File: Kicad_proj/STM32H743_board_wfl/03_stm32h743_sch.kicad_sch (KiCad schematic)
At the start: 1 part, among them U1 STM32H743VITx

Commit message: v0.3 uzupelniony prebom + placement BMI088 na sch
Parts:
- renumbered U1 to U3
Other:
- moved on the sheet: U3
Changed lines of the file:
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@@
 	(symbol
 		(lib_id "MCU_ST_STM32H7:STM32H743VITx")
-		(at 214.884 132.588 0)
+		(at 226.314 136.144 0)
 		(unit 1)
 		(body_style 1)
@@
 		(dnp no)
 		(fields_autoplaced yes)
-		(property "Reference" "U1"
-			(at 219.5673 200.914 0)
+		(property "Reference" "U3"
+			(at 230.9973 204.47 0)
 			(show_name no)
 			(do_not_autoplace no)
@@
 		)
 		(property "Value" "STM32H743VITx"
-			(at 219.5673 203.454 0)
+			(at 230.9973 207.01 0)
 			(show_name no)
 			(do_not_autoplace no)
@@
 		)
 		(property "Footprint" "Package_QFP:LQFP-100_14x14mm_P0.5mm"
-			(at 197.104 198.628 0)
+			(at 208.534 202.184 0)
 			(hide yes)
 			(show_name no)
@@
 		)
 		(property "Datasheet" "https://www.st.com/resource/en/datasheet/stm32h743vi.pdf"
-			(at 214.884 132.588 0)
+			(at 226.314 136.144 0)
 			(hide yes)
 			(show_name no)
@@
 		)
 		(property "Description" "STMicroelectronics Arm Cortex-M7 MCU, 2048KB flash, 1024KB RAM, 480 MHz, 1.71-3.6V, 82 GPIO, LQFP100"
-			(at 214.884 132.588 0)
+			(at 226.314 136.144 0)
 			(hide yes)
 			(show_name no)
@@
 			(project "STM32H743_board_wfl"
 				(path "/3ffbaf01-8fe7-4f96-b685-21b9df9d548a/d99da23c-42db-4338-87a0-b38c4540e099"
-					(reference "U1")
+					(reference "U3")
 					(unit 1)
 				)

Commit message: v0.4c stm
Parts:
- added C12: 4.7uF, Capacitor_SMD:C_0603_1608Metric, symbol Device:C
- added C13, C14, C15, C16, C17, C18, C20, C30: 100nF, Capacitor_SMD:C_0402_1005Metric, symbol Device:C
- added C19: 1uF, Capacitor_SMD:C_0603_1608Metric, symbol Device:C
- added C21, C22: 27pF, Capacitor_SMD:C_0402_1005Metric, symbol Device:C
- added C25, C26: 2.2uF, Capacitor_SMD:C_0603_1608Metric, symbol Device:C
- added JP1: PROG_MODE_JUMPER, Resistor_SMD:R_01005_0402Metric, symbol Jumper:SolderJumper_2_Open
- added L4: BLM21PG221SN1D, Inductor_SMD:L_0805_2012Metric, symbol Device:L_Ferrite
- added R10, R11, R12, R9: 33R, Resistor_SMD:R_01005_0402Metric, symbol Device:R
- added R13: 1k, Resistor_SMD:R_01005_0402Metric, symbol Device:R
- added R5: 10k, Resistor_SMD:R_01005_0402Metric, symbol Device:R
- added R7, R8: 4.7k, Resistor_SMD:R_01005_0402Metric, symbol Device:R
- added Y1: Crystal, Crystal:Crystal_SMD_Abracon_ABM3-2Pin_5.0x3.2mm, symbol Device:Crystal
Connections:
- net GND: now reaches U3.10 (VSS), U3.26 (VSS), U3.49 (VSS), U3.74 (VSS), U3.99 (VSS)
- net GND: now also U3.19 (VSSA), C12.2, C13.2, C14.2, C15.2, C16.2, C17.2, C18.2, C19.2, C20.2, C21.2, C22.2, C25.2, C26.2, C30.2, R5.2
- net +3V3: now reaches U3.100 (VDD)
- net +3V3: now also U3.11 (VDD), U3.27 (VDD), U3.50 (VDD), U3.6 (VBAT), U3.75 (VDD), C12.1, C13.1, C14.1, C15.1, C16.1, C17.1, JP1.2 (B), L4.2, R7.1, R8.1
- net at U3.12 (PH0): now also C21.1, Y1.2
- net at U3.13 (PH1): now also C22.1, Y1.1
- net SWD_NRST: now reaches U3.14 (NRST)
- net SWD_NRST: now also C20.1
- net at U3.20 (VREF+): now also U3.21 (VDDA), C18.1, C19.1, L4.1
- net at U3.22 (PA0): now also C30.1, R13.2
- net UART2_TX: now reaches U3.24 (PA2)
- net UART2_RX: now reaches U3.25 (PA3)
- net CS1_ACCELEROMETER: now reaches U3.28 (PA4)
- net SPI1_SCK: now reaches U3.29 (PA5)
- net SPI1_MISO: now reaches U3.30 (PA6)
- net SPI1_MOSI: now reaches U3.31 (PA7)
- net CS2_GYROSCOPE: now reaches U3.32 (PC4)
- net INT1_ACCELEROMETER: now reaches U3.33 (PC5)
- net INT3_GYROSCOPE: now reaches U3.34 (PB0)
- net FLASH_CLK: now reaches U3.36 (PB2)
- net FLASH_DI/IO0: now reaches U3.37 (PE7)
- net FLASH_DO/IO1: now reaches U3.38 (PE8)
- net FLASH_WP/IO2: now reaches U3.39 (PE9)
- net FLASH_HOLD/RESET/IO3: now reaches U3.40 (PE10)
- net at U3.48 (VCAP): now also U3.73 (VCAP), C25.1, C26.1
- net TELEMETRY: now reaches U3.56 (PD9)
- net at U3.63 (PC6): now also R9.1
- net at U3.64 (PC7): now also R10.1
- net at U3.65 (PC8): now also R11.1
- net at U3.66 (PC9): now also R12.1
- net UART1_TX: now reaches U3.68 (PA9)
- net UART1_RX: now reaches U3.69 (PA10)
- net SWDIO: now reaches U3.72 (PA13)
- net SWCLK: now reaches U3.76 (PA14)
- net FLASH_CS: now reaches U3.79 (PC11)
- net SWO: now reaches U3.89 (PB3)
- net I2C1_SCL: now reaches U3.92 (PB6)
- net I2C1_SCL: now also R7.2
- net I2C1_SDA: now reaches U3.93 (PB7)
- net I2C1_SDA: now also R8.2
- net at U3.94 (BOOT0): now also JP1.1 (A), R5.1
- new net CURRENT: R13.1
- new net MOTOR_1: R9.2
- new net MOTOR_2: R10.2
- new net MOTOR_3: R11.2
- new net MOTOR_4: R12.2
- no-connect marks 0 -> 52

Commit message: v.04d IMU
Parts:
- added J1: GPS, Connector_JST:JST_GH_SM06B-GHS-TB_1x06-1MP_P1.25mm_Horizontal, symbol Connector_Generic:Conn_01x06
- added J2: ESC, Connector_JST:JST_GH_SM08B-GHS-TB_1x08-1MP_P1.25mm_Horizontal, symbol Connector_Generic:Conn_01x08
- added J3: UART, Connector_JST:JST_GH_SM04B-GHS-TB_1x04-1MP_P1.25mm_Horizontal, symbol Connector_Generic:Conn_01x04
- added J4: Tag_Connect_6pin, symbol Connector_Generic:Conn_02x03_Counter_Clockwise
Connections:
- net +3V3: now also J4.1 (Pin_1)
- net CURRENT: now also J2.3 (Pin_3)
- net I2C1_SCL: now also J1.5 (Pin_5)
- net I2C1_SDA: now also J1.6 (Pin_6)
- net MOTOR_1: now also J2.5 (Pin_5)
- net MOTOR_2: now also J2.6 (Pin_6)
- net MOTOR_3: now also J2.7 (Pin_7)
- net MOTOR_4: now also J2.8 (Pin_8)
- net SWCLK: now also J4.4 (Pin_4)
- net SWDIO: now also J4.2 (Pin_2)
- net SWD_NRST: now also J4.3 (Pin_3)
- net SWO: now also J4.6 (Pin_6)
- net TELEMETRY: now also J2.4 (Pin_4)
- net UART1_RX: now also J3.3 (Pin_3)
- net UART1_TX: now also J3.4 (Pin_4)
- net UART2_RX: now also J1.3 (Pin_3)
- net UART2_TX: now also J1.4 (Pin_4)
- net GND renamed -BATT
- net -BATT: now also J1.2 (Pin_2), J2.2 (Pin_2), J3.2 (Pin_2), J4.5 (Pin_5)
- new net +5V: J1.1 (Pin_1), J3.1 (Pin_1)
- new net +BATT: J2.1 (Pin_1)

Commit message: v0.5 schematics + lib update
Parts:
- added C23: 1uF, Capacitor_SMD:C_0603_1608Metric, symbol Device:C
- added C24: 100nF, Capacitor_SMD:C_0402_1005Metric, symbol Device:C
- added R6: 10k, Resistor_SMD:R_01005_0402Metric, symbol Device:R
- added U4: W25Q512JVEIQ, Package_SON:WSON-8-1EP_6x5mm_P1.27mm_EP3.4x4.3mm, symbol STM32H743_board_library_symbols:W25Q512JVEIQ
- Y1: value Crystal -> 8MHz Crystal
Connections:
- net +3V3: now also C23.1, C24.1, R6.1, U4.8 (VCC)
- net -BATT: now also C23.2, C24.2, U4.4 (GND), U4.9 (EP)
- net FLASH_CLK: now also U4.6 (CLK)
- net FLASH_CS: now also R6.2, U4.1 (~{CS})
- net FLASH_DI/IO0: now also U4.5 (DI/IO_{0})
- net FLASH_DO/IO1: now also U4.2 (DO/IO_{1})
- net FLASH_HOLD/RESET/IO3: now also U4.7 (~{HOLD}/~{RESET}/IO_{3})
- net FLASH_WP/IO2: now also U4.3 (~{WP}/IO_{2})

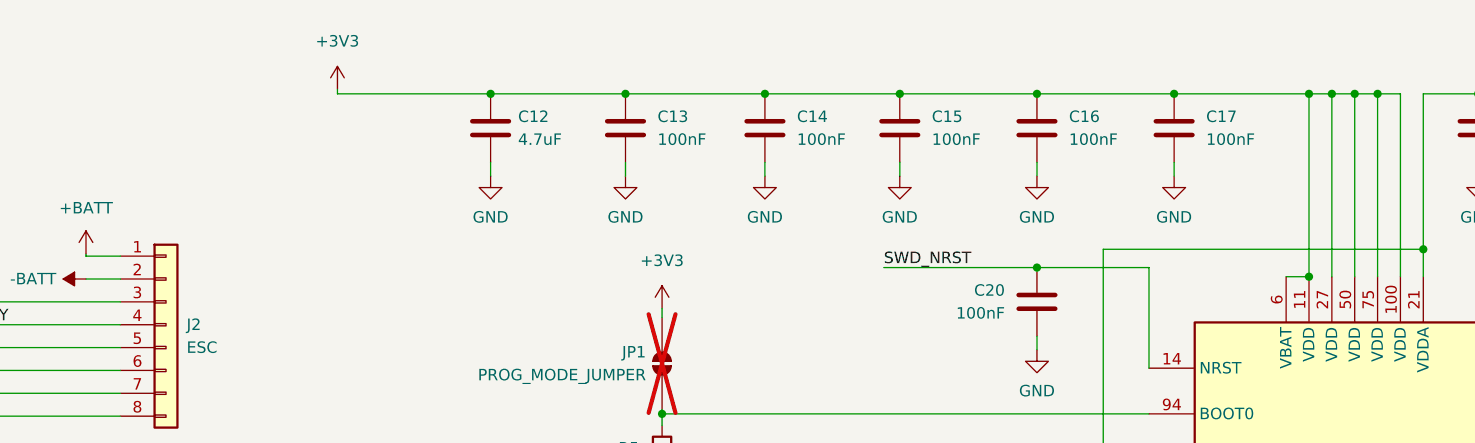
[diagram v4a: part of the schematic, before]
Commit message: v0.5b tvs and stm32 vbat fixes
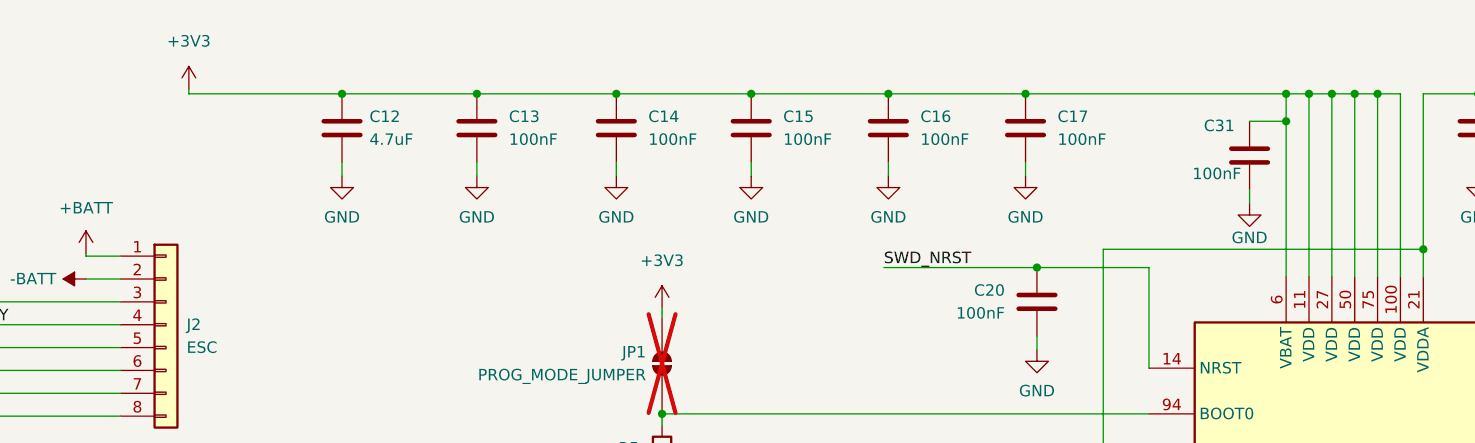
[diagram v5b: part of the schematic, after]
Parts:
- added C31: 100nF, Capacitor_SMD:C_0402_1005Metric, symbol Device:C
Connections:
- net +3V3: now also C31.1
- net -BATT: now also C31.2
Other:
- moved on the sheet: C12, C13, C14, C15, C16, C17

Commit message: v0.5 footprint and lib fixes LT8609
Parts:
- J4: footprint (none) -> Connector:Tag-Connect_TC2030-IDC-NL_2x03_P1.27mm_Vertical
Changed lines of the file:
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@@
 			)
 		)
-		(property "Footprint" ""
+		(property "Footprint" "Connector:Tag-Connect_TC2030-IDC-NL_2x03_P1.27mm_Vertical"
 			(at 80.772 146.05 0)
 			(hide yes)

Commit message: PCB v0.1d components placement STM32 caps
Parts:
- renumbered C31 to C20, C20 to C21, C30 to C22, C21 to C23, C22 to C24, C23 to C27, C24 to C28, L4 to L2, R6 to R13, R13 to R5, R5 to R6
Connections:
- net -BATT renamed GND

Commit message: SCH v0.6b new crystal + library update
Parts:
- Y1: value 8MHz Crystal -> TSX-3225_16.0000MF18X-AC0; footprint Crystal:Crystal_SMD_Abracon_ABM3-2Pin_5.0x3.2mm -> Crystal:Crystal_SMD_3225-4Pin_3.2x2.5mm; symbol Device:Crystal -> STM32H743_board_library_symbols:TSX-3225_16.0000MF18X-AC0
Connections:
- net at C23.1, U3.12 (PH0): now also Y1.3; no longer Y1.2
- new net: Y1.2 (G), Y1.4 (G)
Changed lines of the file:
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@@
 	)
 	(symbol
-		(lib_id "Device:Crystal")
+		(lib_id "STM32H743_board_library_symbols:TSX-3225_16.0000MF18X-AC0")
 		(at 176.276 89.154 90)
 		(unit 1)
@@
 		(in_pos_files yes)
 		(dnp no)
-		(fields_autoplaced yes)
 		(property "Reference" "Y1"
-			(at 180.34 87.8839 90)
+			(at 171.45 87.8839 90)
 			(show_name no)
 			(do_not_autoplace no)
@@
 					(size 1.27 1.27)
 				)
-				(justify right)
+				(justify left)
 			)
 		)
-		(property "Value" "8MHz Crystal"
-			(at 180.34 90.4239 90)
+		(property "Value" "TSX-3225_16.0000MF18X-AC0"
+			(at 192.024 82.804 90)
 			(show_name no)
 			(do_not_autoplace no)
@@
 					(size 1.27 1.27)
 				)
-				(justify right)
+				(justify left)
 			)
 		)
-		(property "Footprint" "Crystal:Crystal_SMD_Abracon_ABM3-2Pin_5.0x3.2mm"
+		(property "Footprint" "Crystal:Crystal_SMD_3225-4Pin_3.2x2.5mm"
 			(at 176.276 89.154 0)
 			(hide yes)
@@
 			)
 		)
-		(property "Datasheet" "https://www.mouser.pl/pl/ProductDetail/ABRACON/ABM3-8.000MHZ-D2Y-T?qs=ihRgKfnEsN4giUXjc3yS1g%3D%3D"
+		(property "Datasheet" "https://www.mouser.pl/pl/ProductDetail/Epson-Timing/TSX-3225-16.0000MF18X-AC0?qs=wwacUt%252BV97taurHtFwy%2FEA%3D%3D"
 			(at 176.276 89.154 0)
 			(hide yes)
@@
 			)
 		)
-		(property "Description" "Two pin crystal"
+		(property "Description" "Four pin crystal, GND on pins 2 and 4"
 			(at 176.276 89.154 0)
 			(hide yes)
@@
 		(pin "1"
 		)
+		(pin "3"
+		)
+		(pin "4"
+		)
 		(instances
